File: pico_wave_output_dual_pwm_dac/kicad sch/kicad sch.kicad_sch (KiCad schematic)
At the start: 4 parts

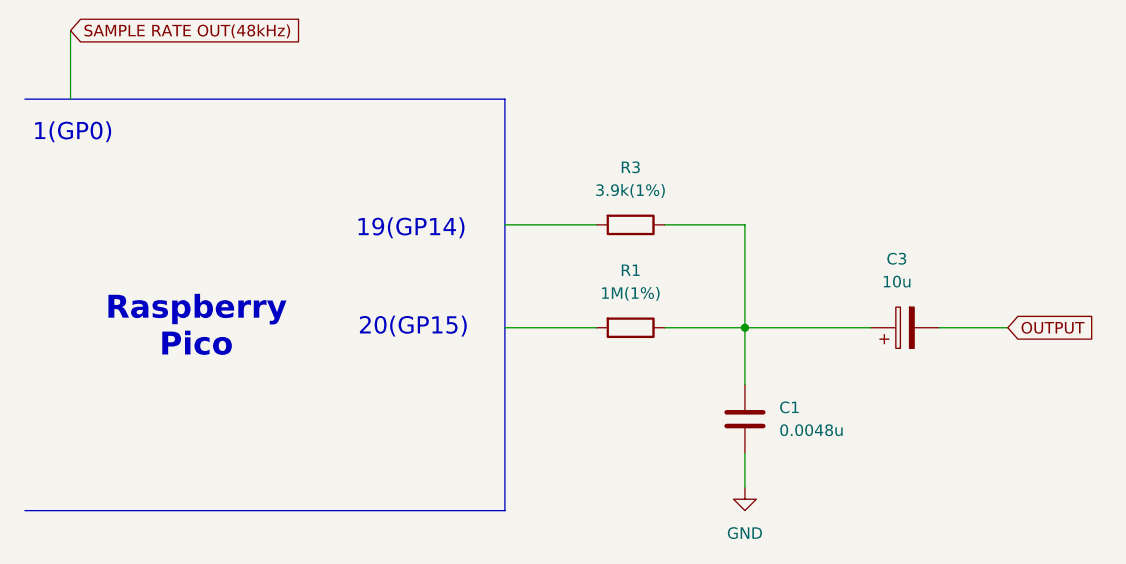
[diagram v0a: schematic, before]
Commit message: Remove obsolete KiCad schematic and backup files; update capacitor value in schematic
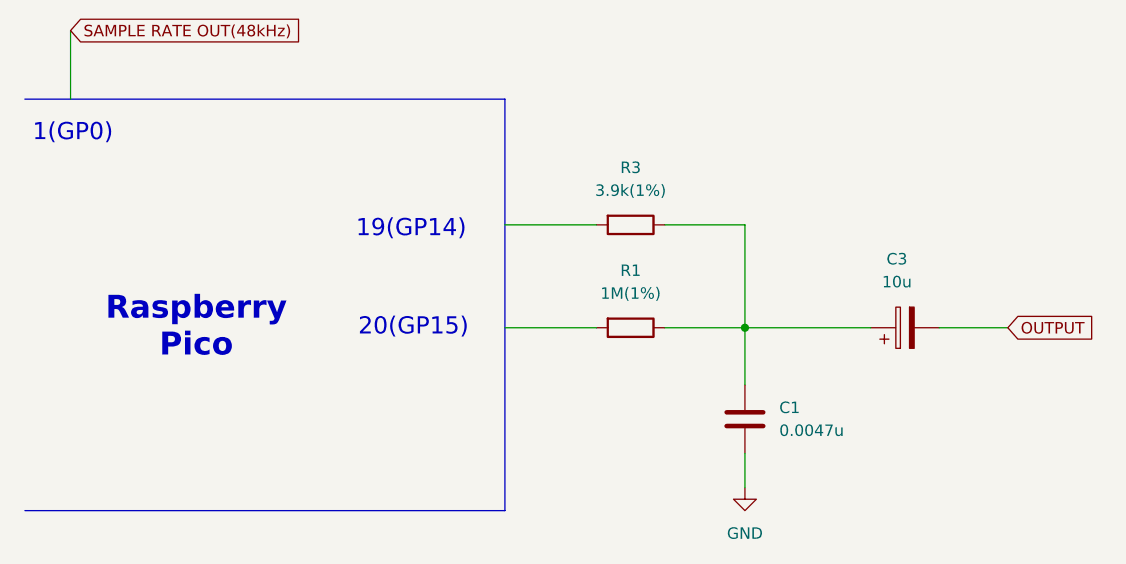
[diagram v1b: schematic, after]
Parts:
- C1: value 0.0048u -> 0.0047u
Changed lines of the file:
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@@
 			)
 		)
-		(property "Value" "0.0048u"
+		(property "Value" "0.0047u"
 			(at 160.02 100.3299 0)
 			(effects
